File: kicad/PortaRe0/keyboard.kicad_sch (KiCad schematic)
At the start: 158 parts, among them J1 StickSocket, U6 RP2040#1, Y2 12Mhz

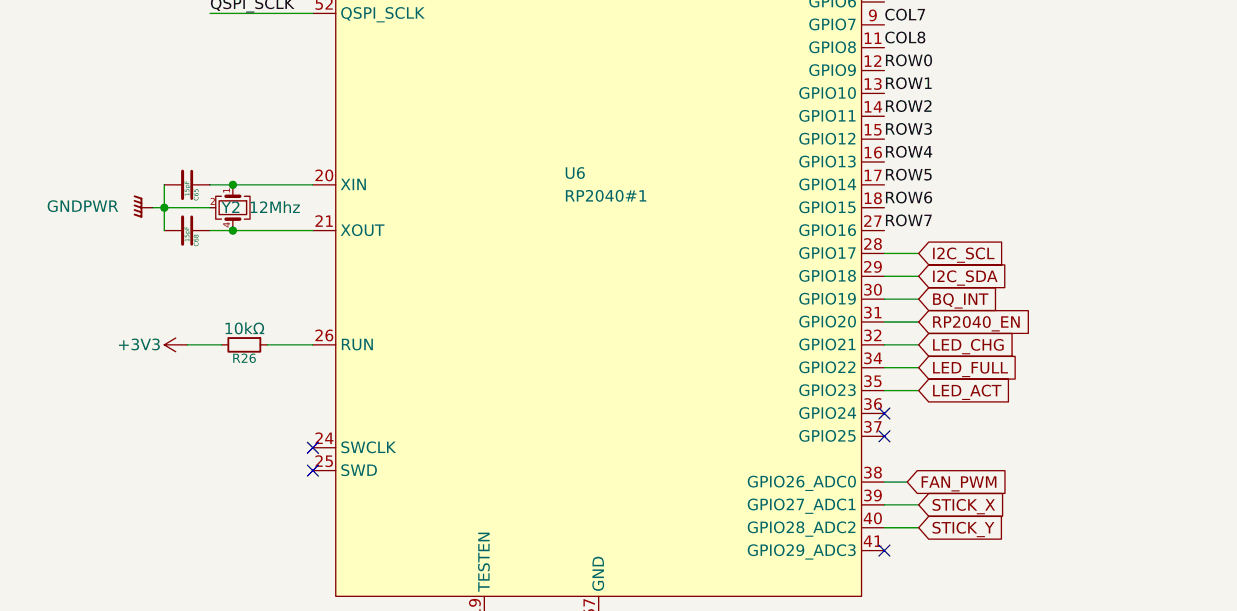
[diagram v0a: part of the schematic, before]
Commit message: KiCad/Docs: チェックシート04-06完了・回路修正(session25)
- VL812: W25Q32 /CS GNDプルダウン→3V3_HUBプルアップ修正
- RP2040 #1/#2: クリスタルシンボル GND23→GND24 修正
- RP2040 #1: GP24/GP25 接続追加
- チェックシート04(VL812)/05(RP2040 kbd)/06(RP2040 audio)記入完了

Co-Authored-By: Claude Sonnet 4.6 <noreply@anthropic.com>
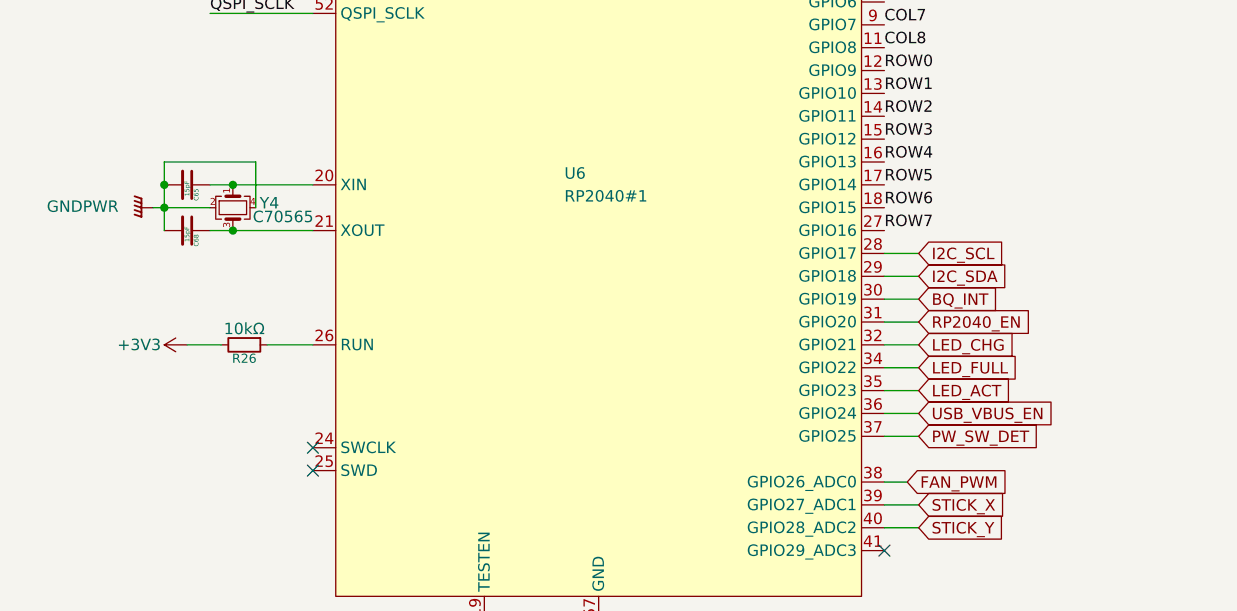
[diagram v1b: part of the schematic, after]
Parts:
- removed Y2: 12Mhz, Crystal:Crystal_SMD_3225-4Pin_3.2x2.5mm, symbol Device:Crystal_GND23_Small
- added Y4: C70565, symbol Device:Crystal_GND24_Small
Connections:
- net GNDPWR: now also Y4.2, Y4.4
- net at C65.1, U6.20 (XIN): now also Y4.1
- net at C68.1, U6.21 (XOUT): now also Y4.3
- net USB_VBUS_EN: now reaches U6.36 (GPIO24)
- net PW_SW_DET: now reaches U6.37 (GPIO25)
- no-connect marks 5 -> 3
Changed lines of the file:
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@@
 	)
 	(junction
+		(at 67.31 173.99)
+		(diameter 0)
+		(color 0 0 0 0)
+	)
+	(junction
 		(at 264.16 158.75)
 		(diameter 0)
@@
 	)
 	(junction
-		(at 67.31 179.07)
+		(at 59.69 173.99)
 		(diameter 0)
 		(color 0 0 0 0)
@@
 	)
 	(junction
+		(at 67.31 179.07)
+		(diameter 0)
+		(color 0 0 0 0)
+	)
+	(junction
 		(at 254 107.95)
 		(diameter 0)
@@
 	)
 	(junction
-		(at 67.31 173.99)
-		(diameter 0)
-		(color 0 0 0 0)
-	)
-	(junction
 		(at 198.12 93.98)
 		(diameter 0)
@@
 	)
 	(no_connect
-		(at 139.7 199.39)
-	)
-	(no_connect
 		(at 76.2 203.2)
 	)
 	(no_connect
-		(at 139.7 201.93)
-	)
-	(no_connect
 		(at 76.2 205.74)
 	)
@@
 	(wire
 		(pts
+			(xy 59.69 171.45) (xy 59.69 173.99)
+		)
+		(stroke
+			(width 0)
+			(type default)
+		)
+	)
+	(wire
+		(pts
 			(xy 101.6 102.87) (xy 101.6 107.95)
 		)
@@
 	(wire
 		(pts
+			(xy 67.31 173.99) (xy 76.2 173.99)
+		)
+		(stroke
+			(width 0)
+			(type default)
+		)
+	)
+	(wire
+		(pts
 			(xy 222.25 102.87) (xy 222.25 116.84)
 		)
@@
 	(wire
 		(pts
-			(xy 67.31 179.07) (xy 76.2 179.07)
+			(xy 240.03 93.98) (xy 254 93.98)
 		)
 		(stroke
@@
 	(wire
 		(pts
-			(xy 240.03 93.98) (xy 254 93.98)
+			(xy 189.23 193.04) (xy 190.5 193.04)
 		)
 		(stroke
@@
 	(wire
 		(pts
-			(xy 189.23 193.04) (xy 190.5 193.04)
+			(xy 278.13 102.87) (xy 278.13 116.84)
 		)
 		(stroke
@@
 	(wire
 		(pts
-			(xy 278.13 102.87) (xy 278.13 116.84)
+			(xy 198.12 127) (xy 198.12 130.81)
 		)
 		(stroke
@@
 	(wire
 		(pts
-			(xy 198.12 127) (xy 198.12 130.81)
+			(xy 67.31 179.07) (xy 76.2 179.07)
+		)
+		(stroke
+			(width 0)
+			(type default)
+		)
+	)
+	(wire
+		(pts
+			(xy 143.51 201.93) (xy 139.7 201.93)
 		)
 		(stroke
@@
 	(wire
 		(pts
-			(xy 67.31 173.99) (xy 76.2 173.99)
+			(xy 64.77 173.99) (xy 67.31 173.99)
 		)
 		(stroke
@@
 	(wire
 		(pts
-			(xy 64.77 173.99) (xy 67.31 173.99)
-		)
-		(stroke
-			(width 0)
-			(type default)
-		)
-	)
-	(wire
-		(pts
 			(xy 320.04 130.81) (xy 320.04 144.78)
 		)
@@
 	(wire
 		(pts
+			(xy 69.85 171.45) (xy 59.69 171.45)
+		)
+		(stroke
+			(width 0)
+			(type default)
+		)
+	)
+	(wire
+		(pts
 			(xy 95.25 102.87) (xy 95.25 99.06)
 		)
@@
 	(wire
 		(pts
+			(xy 143.51 199.39) (xy 139.7 199.39)
+		)
+		(stroke
+			(width 0)
+			(type default)
+		)
+	)
+	(wire
+		(pts
 			(xy 254 154.94) (xy 254 158.75)
 		)
@@
 	(wire
 		(pts
+			(xy 69.85 176.53) (xy 69.85 171.45)
+		)
+		(stroke
+			(width 0)
+			(type default)
+		)
+	)
+	(wire
+		(pts
 			(xy 143.51 212.09) (xy 139.7 212.09)
 		)
@@
 		)
 	)
+	(global_label "PW_SW_DET"
+		(shape input)
+		(at 143.51 201.93 0)
+		(fields_autoplaced yes)
+		(effects
+			(font
+				(size 1.27 1.27)
+			)
+			(justify left)
+		)
+		(property "Intersheetrefs" "${INTERSHEET_REFS}"
+			(at 157.1993 201.93 0)
+			(effects
+				(font
+					(size 1.27 1.27)
+				)
+				(justify left)
+				(hide yes)
+			)
+		)
+	)
 	(global_label "STICK_X"
 		(shape input)
@@
 		)
 	)
+	(global_label "USB_VBUS_EN"
+		(shape input)
+		(at 143.51 199.39 0)
+		(fields_autoplaced yes)
+		(effects
+			(font
+				(size 1.27 1.27)
+			)
+			(justify left)
+		)
+		(property "Intersheetrefs" "${INTERSHEET_REFS}"
+			(at 159.6185 199.39 0)
+			(effects
+				(font
+					(size 1.27 1.27)
+				)
+				(justify left)
+				(hide yes)
+			)
+		)
+	)
 	(global_label "I2C_SCL"
 		(shape input)
@@
 	)
 	(symbol
-		(lib_id "Device:Crystal_GND23_Small")
-		(at 67.31 176.53 270)
-		(unit 1)
-		(exclude_from_sim no)
-		(in_bom yes)
-		(on_board yes)
-		(dnp no)
-		(property "Reference" "Y2"
-			(at 66.04 176.53 90)
-			(effects
-				(font
-					(size 1.27 1.27)
-				)
-				(justify left)
-			)
-		)
-		(property "Value" "12Mhz"
-			(at 69.088 176.53 90)
-			(effects
-				(font
-					(size 1.27 1.27)
-				)
-				(justify left)
-			)
-		)
-		(property "Footprint" "Crystal:Crystal_SMD_3225-4Pin_3.2x2.5mm"
-			(at 67.31 176.53 0)
-			(effects
-				(font
-					(size 1.27 1.27)
-				)
-				(hide yes)
-			)
-		)
-		(property "Datasheet" "~"
-			(at 67.31 176.53 0)
-			(effects
-				(font
-					(size 1.27 1.27)
-				)
-				(hide yes)
-			)
-		)
-		(property "Description" "Four pin crystal, GND on pins 2 and 3, small symbol"
-			(at 57.15 176.53 0)
-			(effects
-				(font
-					(size 1.27 1.27)
-				)
-				(hide yes)
-			)
-		)
-		(property private "KLC_S4.1" "Some pins are on 50mil grid to make the symbol small"
-			(at 48.26 176.53 0)
-			(show_name yes)
-			(effects
-				(font
-					(size 1.27 1.27)
-				)
-				(hide yes)
-			)
-		)
-		(property private "KLC_S3.3" "The rectangle is not a symbol body but a graphical element"
-			(at 50.8 177.8 0)
-			(show_name yes)
-			(effects
-				(font
-					(size 1.27 1.27)
-				)
-				(hide yes)
-			)
-		)
-		(pin "4"
-		)
-		(pin "3"
-		)
-		(pin "1"
-		)
-		(pin "2"
-		)
-		(instances
-			(project ""
-				(path "/479aadc4-f9a0-4ec2-b000-6a17237038f1/6a589eb8-1cb5-4d2d-b60c-ea2cdc8e2546"
-					(reference "Y2")
-					(unit 1)
-				)
-			)
-		)
-	)
-	(symbol
 		(lib_id "Switch:SW_Push")
 		(at 273.05 144.78 0)
@@
 					(unit 1)
 				)
+			)
+		)
+	)
+	(symbol
+		(lib_id "Device:Crystal_GND24_Small")
+		(at 67.31 176.53 270)
+		(unit 1)
+		(exclude_from_sim no)
+		(in_bom yes)
+		(on_board yes)
+		(dnp no)
+		(property "Reference" "Y4"
+			(at 71.374 176.022 90)
+			(effects
+				(font
+					(size 1.27 1.27)
+				)
+			)
+		)
+		(property "Value" "C70565"
+			(at 72.898 177.546 90)
+			(effects
+				(font
+					(size 1.27 1.27)
+				)
+			)
+		)
+		(property "Footprint" ""
+			(at 67.31 176.53 0)
+			(effects
+				(font
+					(size 1.27 1.27)
+				)
+				(hide yes)
+			)
+		)
+		(property "Datasheet" "~"
+			(at 67.31 176.53 0)
+			(effects
+				(font
+					(size 1.27 1.27)
+				)
+				(hide yes)
+			)
+		)
+		(property "Description" "Four pin crystal, GND on pins 2 and 4, small symbol"
+			(at 67.31 176.53 0)
+			(effects
+				(font
+					(size 1.27 1.27)
+				)
+				(hide yes)
+			)
+		)
+		(pin "2"
+		)
+		(pin "1"
+		)
+		(pin "3"
+		)
+		(pin "4"
+		)
+		(instances
+			(project "PortaRe0"
+				(path "/479aadc4-f9a0-4ec2-b000-6a17237038f1/6a589eb8-1cb5-4d2d-b60c-ea2cdc8e2546"
+					(reference "Y4")
+					(unit 1)
+				)

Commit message: KiCad/Docs: session30終了処理・フットプリント割り当て完了・コネクタ確定
- フットプリント全割り当て完了（全シート）
- 新規フットプリント追加: SKSCLBE010/SKRPABE010/クリスタル/インダクタ×3/JST PHコネクタ×2
- コネクタ確定: バッテリー=B8B-PH-K-S(C157974) / SPK+FAN=B2B-PH-K-S(C131337)
- J5(hdmi_adapter): PinHeader_2x08_P2.00mm_Vertical
- Claude.md: ファン制御 RP2040 #1 GP26→BSS138→J6 に更新
- passive_parts.txt: コネクタセクション追加

Co-Authored-By: Claude Sonnet 4.6 <noreply@anthropic.com>
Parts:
- C49, C50, C51, C54, C55, C56, C57, C60, C61, C62, C63, C64, C65, C68, C69: footprint (none) -> Capacitor_SMD:C_0603_1608Metric
- D2, D3, D4: footprint (none) -> LED_SMD:LED_0603_1608Metric
- K_SW1, K_SW2: footprint (none) -> PortaRe0:KEY-SMD_4P-SKSCLXX010
- K_SW10, K_SW11, K_SW12, K_SW13, K_SW14, K_SW15, K_SW16, K_SW17, K_SW18, K_SW19, K_SW20, K_SW21, K_SW22, K_SW23, K_SW24, K_SW25, K_SW26, K_SW27, K_SW28, K_SW29, K_SW3, K_SW30, K_SW31, K_SW32, K_SW33, K_SW34, K_SW35, K_SW36, K_SW37, K_SW38, K_SW39, K_SW4, K_SW40, K_SW41, K_SW42, K_SW43, K_SW44, K_SW45, K_SW46, K_SW47, K_SW48, K_SW49, K_SW5, K_SW50, K_SW51, K_SW52, K_SW53, K_SW54, K_SW55, K_SW56, K_SW57, K_SW58, K_SW59, K_SW6, K_SW60, K_SW61, K_SW62, K_SW63, K_SW64, K_SW7, K_SW8, K_SW9: footprint (none) -> PortaRe0:KEY-SMD_4P-L4.2-W3.2-P2.20-LS4.6
- R26, R27, R28, R29, R30, R31, R32, R33, R34: footprint (none) -> Resistor_SMD:R_0603_1608Metric
- SW_D1, SW_D10, SW_D11, SW_D12, SW_D13, SW_D14, SW_D15, SW_D16, SW_D17, SW_D18, SW_D19, SW_D2, SW_D20, SW_D21, SW_D22, SW_D23, SW_D24, SW_D25, SW_D26, SW_D27, SW_D28, SW_D29, SW_D3, SW_D30, SW_D31, SW_D32, SW_D33, SW_D34, SW_D35, SW_D36, SW_D37, SW_D38, SW_D39, SW_D4, SW_D40, SW_D41, SW_D42, SW_D43, SW_D44, SW_D45, SW_D46, SW_D47, SW_D48, SW_D49, SW_D5, SW_D50, SW_D51, SW_D52, SW_D53, SW_D54, SW_D55, SW_D56, SW_D57, SW_D58, SW_D59, SW_D6, SW_D60, SW_D61, SW_D62, SW_D63, SW_D7, SW_D8, SW_D9: footprint (none) -> PortaRe0:SOD-123_L2.8-W1.8-LS3.7-RD
- Y4: footprint (none) -> PortaRe0:CONN-TH_B2B-PH-K-S

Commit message: Docs/KiCad: session31終了処理・PROGRESS/index更新
- キルスイッチ確定: MSK12C02(C431540) EN制御方式・KiCad配線完了
- ヘッドフォンジャック確定: PJ-307C(C16684) TH / 配線・pull-up完了
- J4バッテリーコネクタ: S8B-PH-K-S-LF-SN(C157915) 水平型確定
- BOM Y4フットプリント修正
- 新規ライブラリ追加: MSK12C02/PJ-307C/S8B-PH-K-S他
- Phase 2 回路設計 全シート完了

Co-Authored-By: Claude Sonnet 4.6 <noreply@anthropic.com>
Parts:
- Y4: footprint PortaRe0:CONN-TH_B2B-PH-K-S -> PortaRe0:CRYSTAL-SMD_4P-L3.2-W2.5-BL
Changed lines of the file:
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@@
 			)
 		)
-		(property "Footprint" "PortaRe0:CONN-TH_B2B-PH-K-S"
+		(property "Footprint" "PortaRe0:CRYSTAL-SMD_4P-L3.2-W2.5-BL"
 			(at 67.31 176.53 0)
 			(effects
